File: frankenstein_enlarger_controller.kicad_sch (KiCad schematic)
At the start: 7 parts

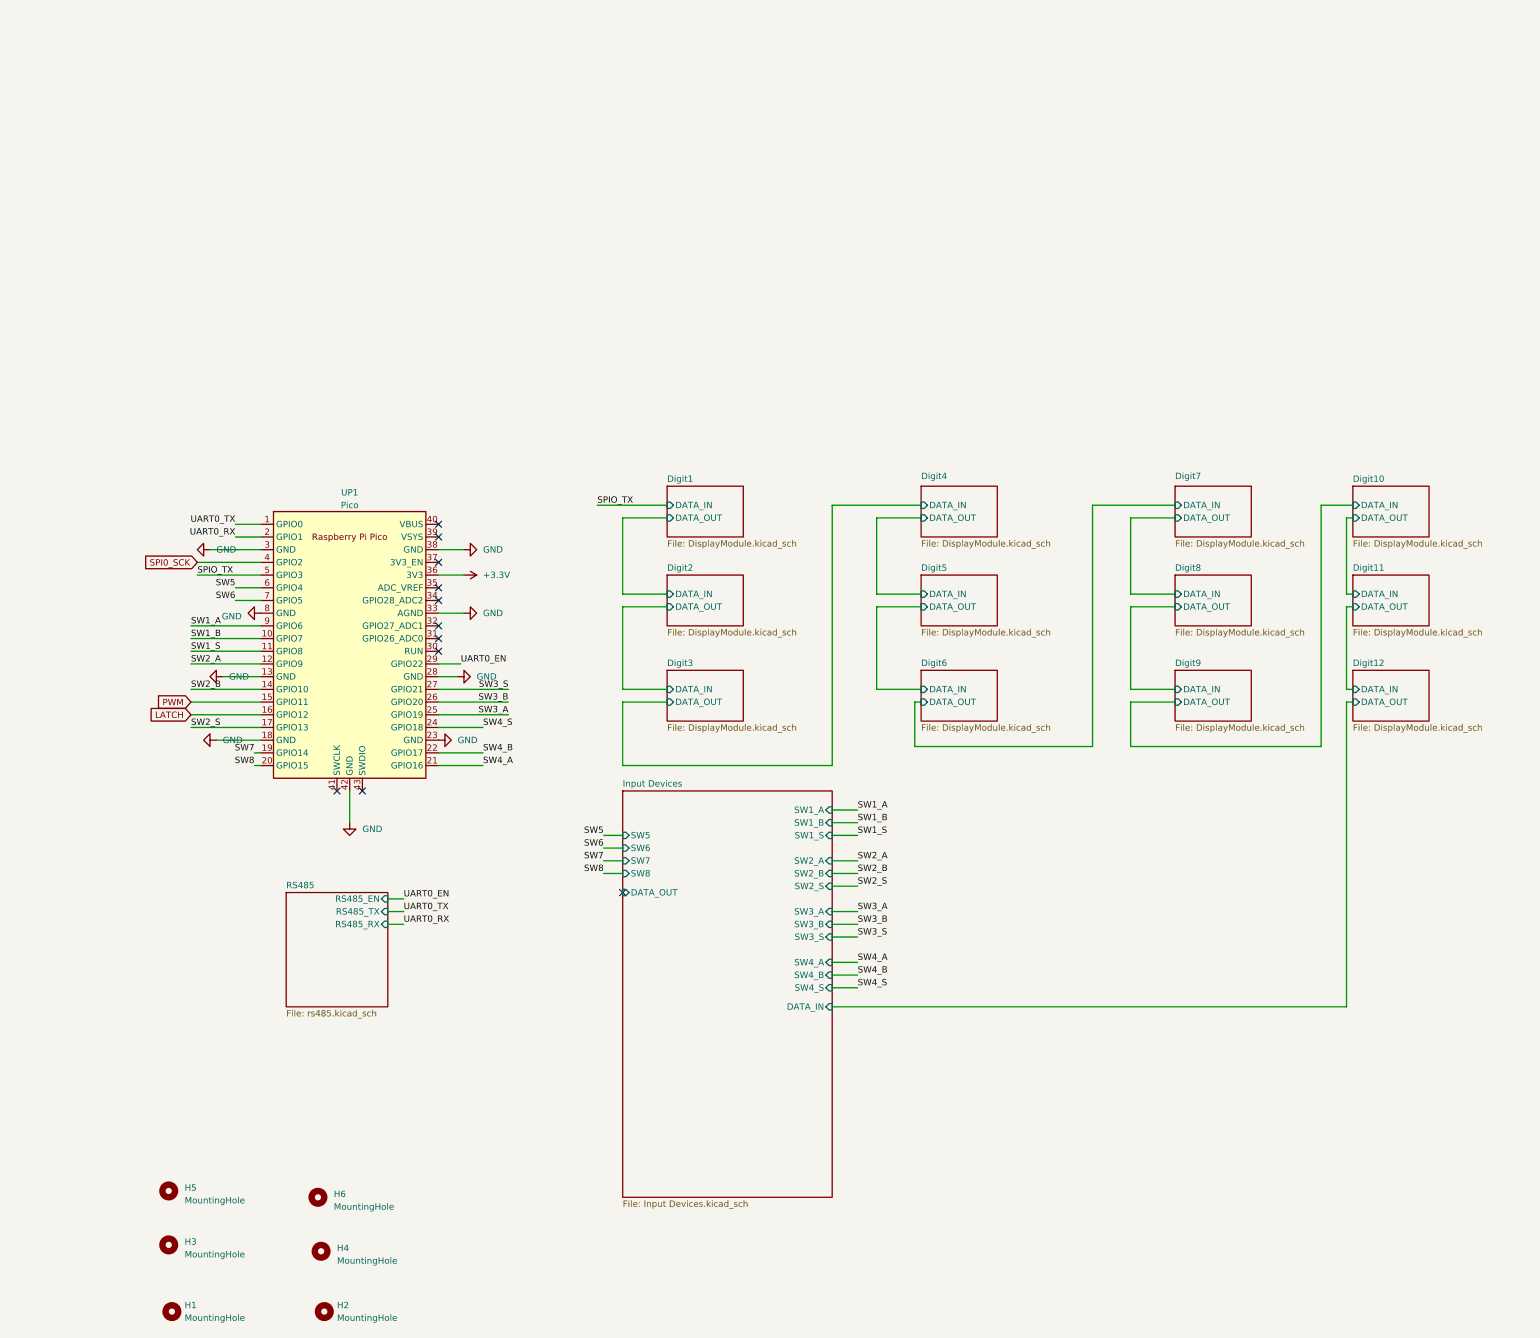
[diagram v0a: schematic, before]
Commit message: First maybe complete version?
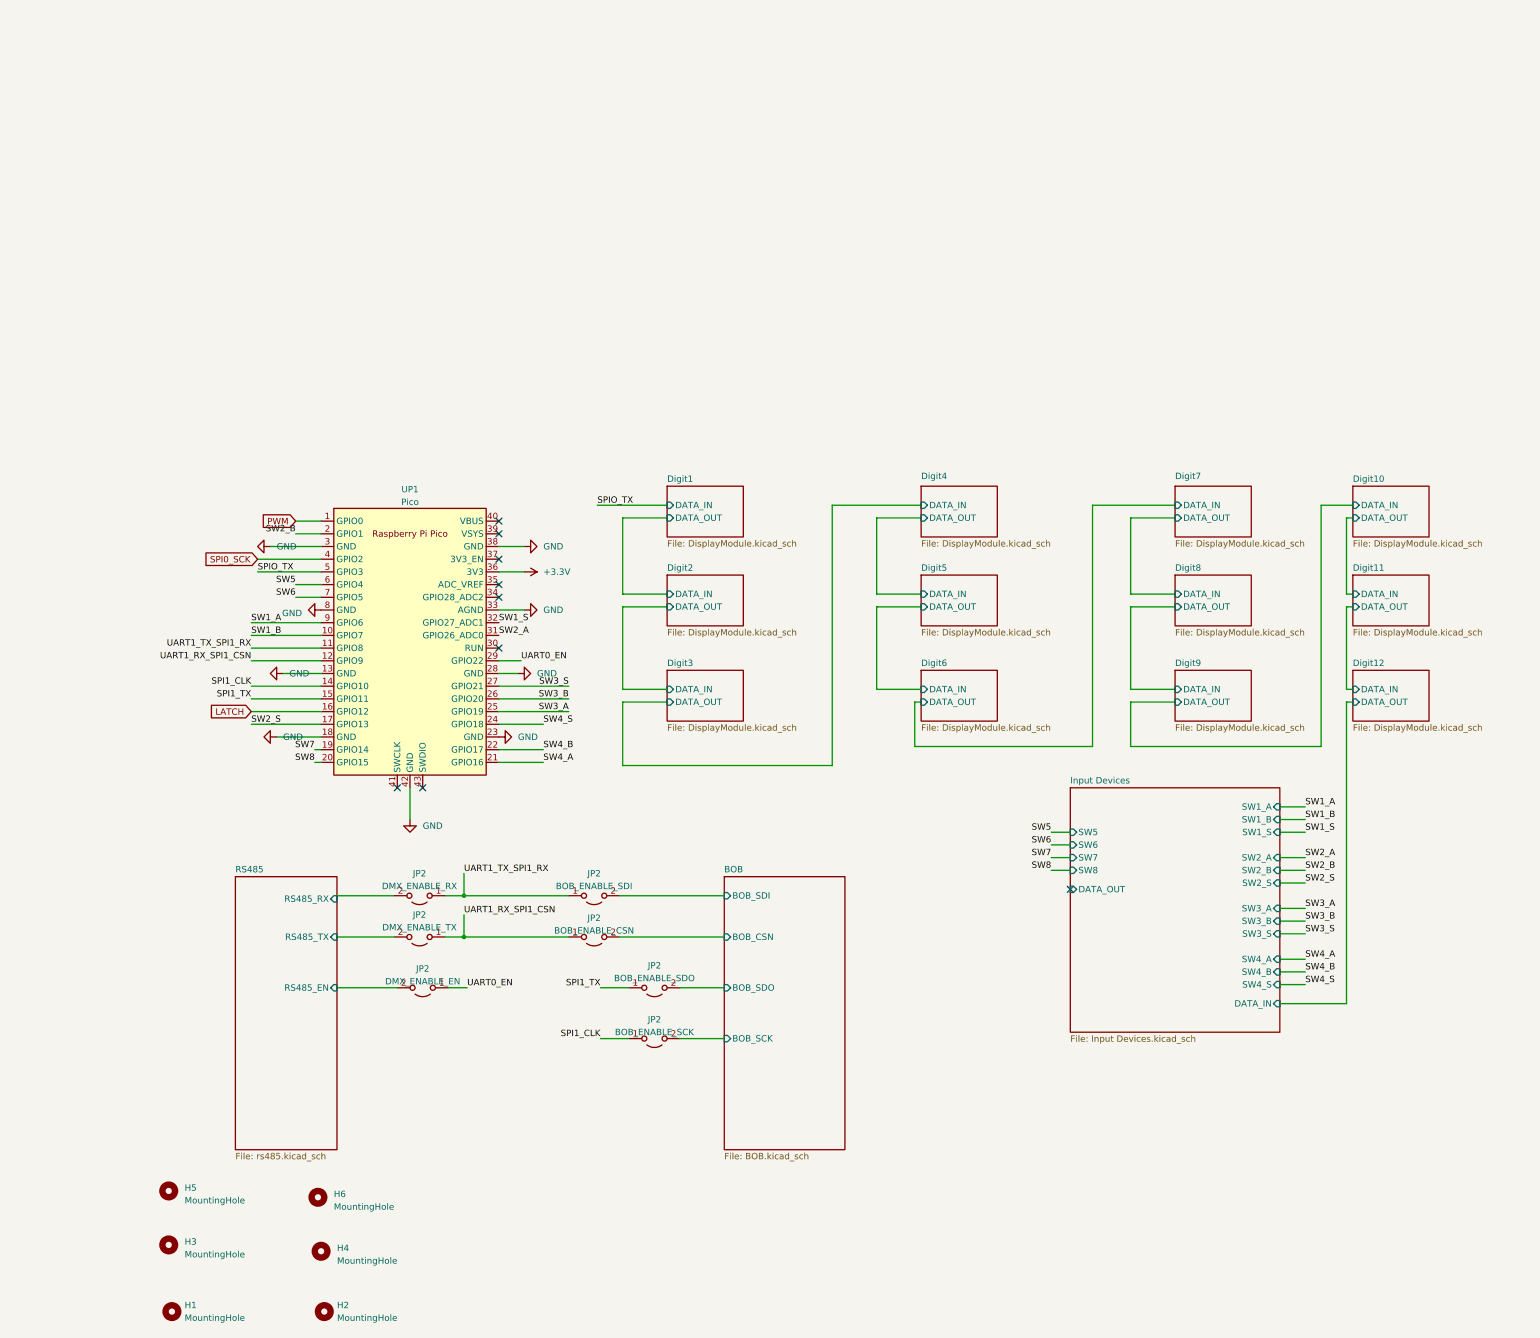
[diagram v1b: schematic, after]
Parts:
- added JP2: BOB_ENABLE_SDO, Jumper:SolderJumper-2_P1.3mm_Open_RoundedPad1.0x1.5mm, symbol Jumper:Jumper_2_Open
- added JP2: BOB_ENABLE_SCK, Jumper:SolderJumper-2_P1.3mm_Open_RoundedPad1.0x1.5mm, symbol Jumper:Jumper_2_Open
- added JP2: DMX_ENABLE_RX, Jumper:SolderJumper-2_P1.3mm_Open_RoundedPad1.0x1.5mm, symbol Jumper:Jumper_2_Open
- added JP2: DMX_ENABLE_TX, Jumper:SolderJumper-2_P1.3mm_Open_RoundedPad1.0x1.5mm, symbol Jumper:Jumper_2_Open
- added JP2: BOB_ENABLE_SDI, Jumper:SolderJumper-2_P1.3mm_Open_RoundedPad1.0x1.5mm, symbol Jumper:Jumper_2_Open
- added JP2: BOB_ENABLE_CSN, Jumper:SolderJumper-2_P1.3mm_Open_RoundedPad1.0x1.5mm, symbol Jumper:Jumper_2_Open
- added JP2: DMX_ENABLE_EN, Jumper:SolderJumper-2_P1.3mm_Open_RoundedPad1.0x1.5mm, symbol Jumper:Jumper_2_Open
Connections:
- net UART0_RX is gone; now on net SW2_B: UP1.2 (GPIO1)
- net UART0_TX is gone; now on net PWM: UP1.1 (GPIO0)
- net PWM: no longer UP1.15 (GPIO11)
- net SW1_S: now also UP1.32 (GPIO27_ADC1); no longer UP1.11 (GPIO8)
- net SW2_A: now also UP1.31 (GPIO26_ADC0); no longer UP1.12 (GPIO9)
- net SW2_B: no longer UP1.14 (GPIO10)
- net UART0_EN: now also JP2.1 (A)
- new net BOB/BOB_CSN: JP2.2 (B)
- new net BOB/BOB_SCK: JP2.2 (B)
- new net BOB/BOB_SDI: JP2.2 (B)
- new net BOB/BOB_SDO: JP2.2 (B)
- new net RS485/RS485_EN: JP2.2 (B)
- new net RS485/RS485_RX: JP2.2 (B)
- new net RS485/RS485_TX: JP2.2 (B)
- new net SPI1_CLK: JP2.1 (A), UP1.14 (GPIO10)
- new net SPI1_TX: JP2.1 (A), UP1.15 (GPIO11)
- new net UART1_RX_SPI1_CSN: JP2.1 (A), JP2.1 (A), UP1.12 (GPIO9)
- new net UART1_TX_SPI1_RX: JP2.1 (A), JP2.1 (A), UP1.11 (GPIO8)
- no-connect marks 11 -> 9
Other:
- added sheet BOB (BOB.kicad_sch)
- moved on the sheet: UP1

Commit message: Consolidated Hardware on single board
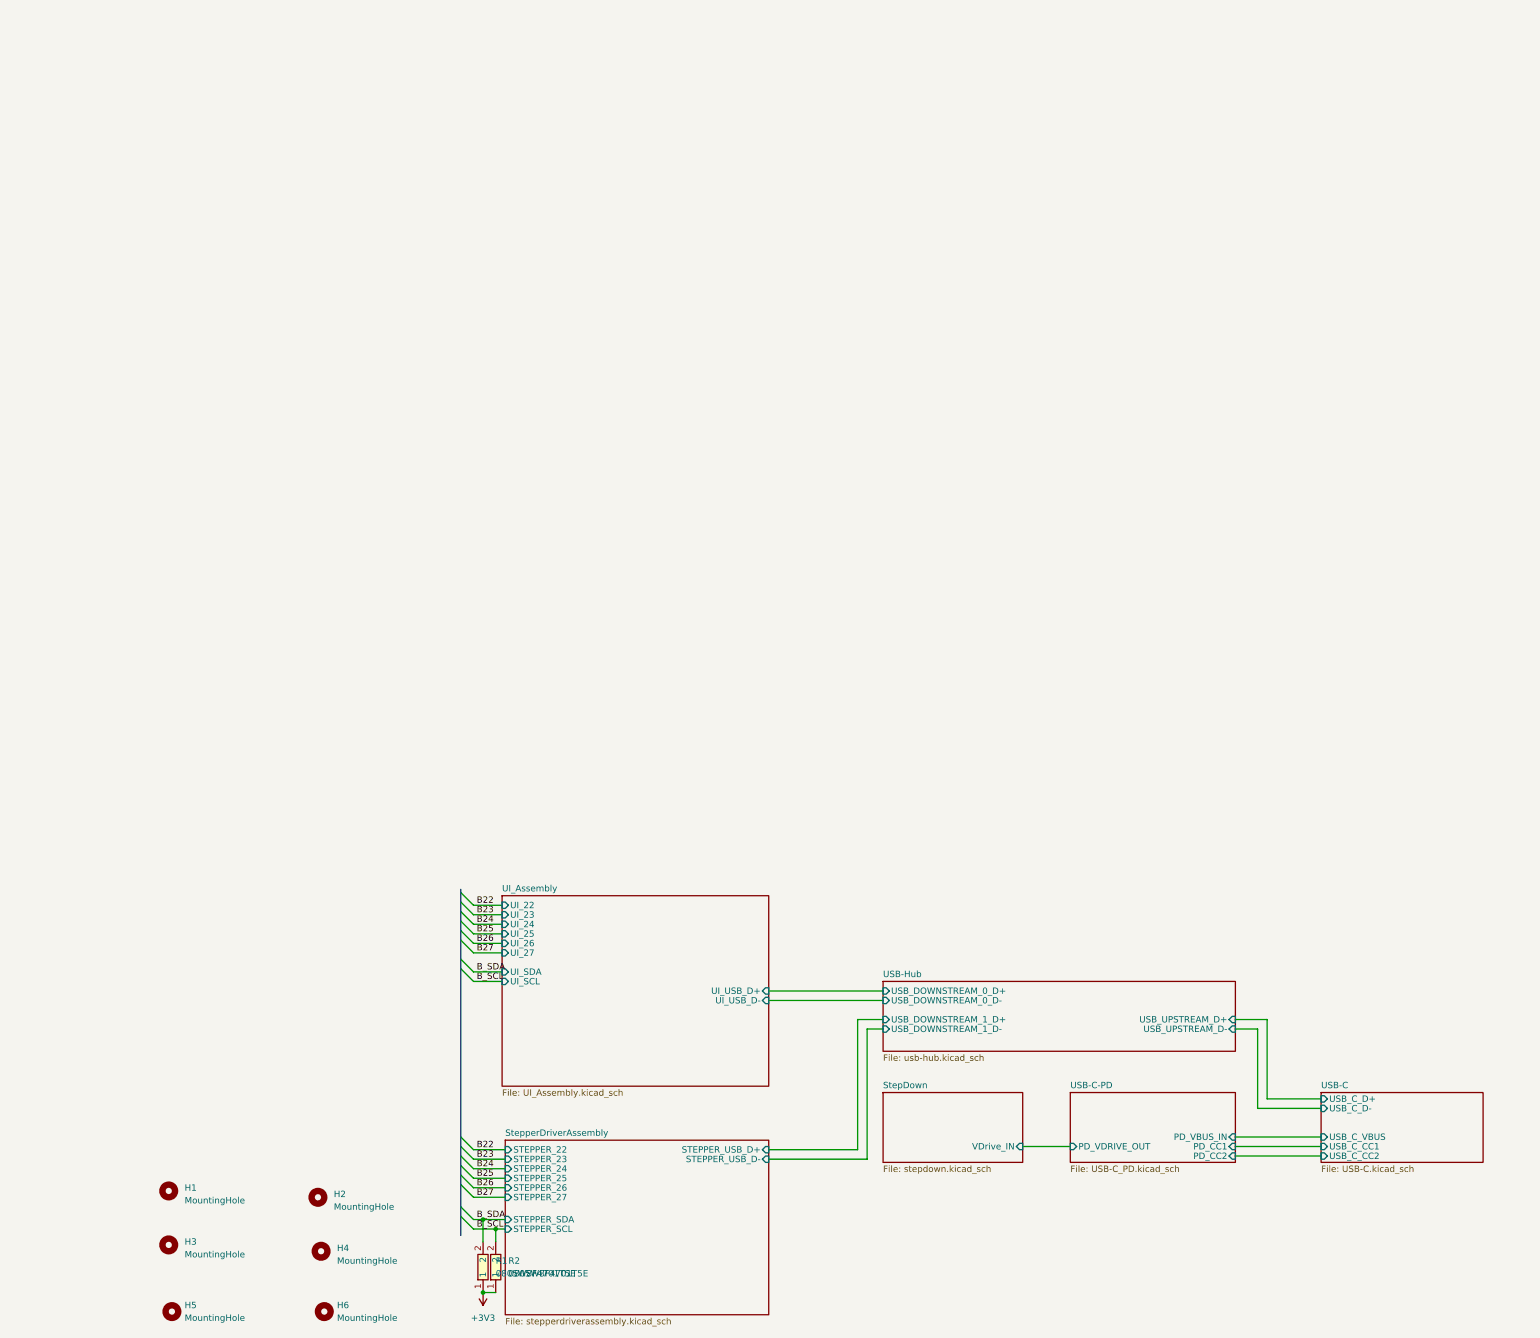
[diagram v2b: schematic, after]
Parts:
- removed JP2: BOB_ENABLE_SDO, Jumper:SolderJumper-2_P1.3mm_Open_RoundedPad1.0x1.5mm, symbol Jumper:Jumper_2_Open
- removed JP2: BOB_ENABLE_SCK, Jumper:SolderJumper-2_P1.3mm_Open_RoundedPad1.0x1.5mm, symbol Jumper:Jumper_2_Open
- removed JP2: DMX_ENABLE_RX, Jumper:SolderJumper-2_P1.3mm_Open_RoundedPad1.0x1.5mm, symbol Jumper:Jumper_2_Open
- removed JP2: DMX_ENABLE_TX, Jumper:SolderJumper-2_P1.3mm_Open_RoundedPad1.0x1.5mm, symbol Jumper:Jumper_2_Open
- removed JP2: BOB_ENABLE_SDI, Jumper:SolderJumper-2_P1.3mm_Open_RoundedPad1.0x1.5mm, symbol Jumper:Jumper_2_Open
- removed JP2: BOB_ENABLE_CSN, Jumper:SolderJumper-2_P1.3mm_Open_RoundedPad1.0x1.5mm, symbol Jumper:Jumper_2_Open
- removed JP2: DMX_ENABLE_EN, Jumper:SolderJumper-2_P1.3mm_Open_RoundedPad1.0x1.5mm, symbol Jumper:Jumper_2_Open
- removed UP1: Pico, MCU_RaspberryPi_and_Boards:RPi_Pico_SMD_TH, symbol MCU_RaspberryPi_and_Boards:Pico
- added R1, R2: 0805W8F4701T5E, easyeda2kicad:R0805, symbol easyeda2kicad:0805W8F4701T5E
- renumbered H5 to H1, H6 to H2, H1 to H5, H2 to H6
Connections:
- new net +3V3: R1.1, R2.1
- new net B_SCL: R2.2
- new net B_SDA: R1.2
- no-connect marks 9 -> 0
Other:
- removed sheet BOB
- removed sheet Digit1
- removed sheet Digit10
- removed sheet Digit11
- removed sheet Digit12
- removed sheet Digit2
- removed sheet Digit3
- removed sheet Digit4
- removed sheet Digit5
- removed sheet Digit6
- removed sheet Digit7
- removed sheet Digit8
- removed sheet Digit9
- removed sheet Input Devices
- removed sheet RS485
- added sheet StepDown (stepdown.kicad_sch)
- added sheet StepperDriverAssembly (stepperdriverassembly.kicad_sch)
- added sheet UI_Assembly (UI_Assembly.kicad_sch)
- added sheet USB-C (USB-C.kicad_sch)
- added sheet USB-C-PD (USB-C_PD.kicad_sch)
- added sheet USB-Hub (usb-hub.kicad_sch)
- company: (none) -> wirkbetrieb.net / Tom Eichhorn
- title: (none) -> Frankenstein Controller

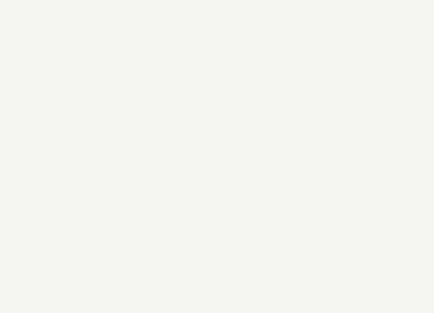
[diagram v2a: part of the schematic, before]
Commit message: Tie VBUS_FET_EN and SAFE_PWR_EN together
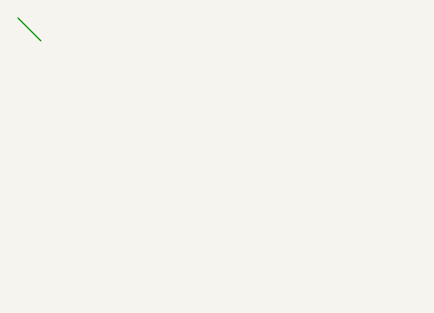
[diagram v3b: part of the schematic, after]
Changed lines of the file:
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@@
+    (stroke (width 0) (type default))
+  )
+  (bus_entry (at -13.335 -71.12) (size 2.54 2.54)
     (stroke (width 0) (type default))
   )
